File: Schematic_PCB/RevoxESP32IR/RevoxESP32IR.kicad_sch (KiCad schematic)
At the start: 27 parts, among them J1 SerialLink, J2 Conn_01x04, J3 Conn_01x10, J4 Conn_01x05, J5 Conn_01x04, J6 Conn_01x03, Q1 BC550, Q2 2N2222, Q3 BC550, U1 esp32-wemos-d1-mini, U2 TSOP331xx, U3 TTL-RS232 Modul, U6 FXMA108_THT

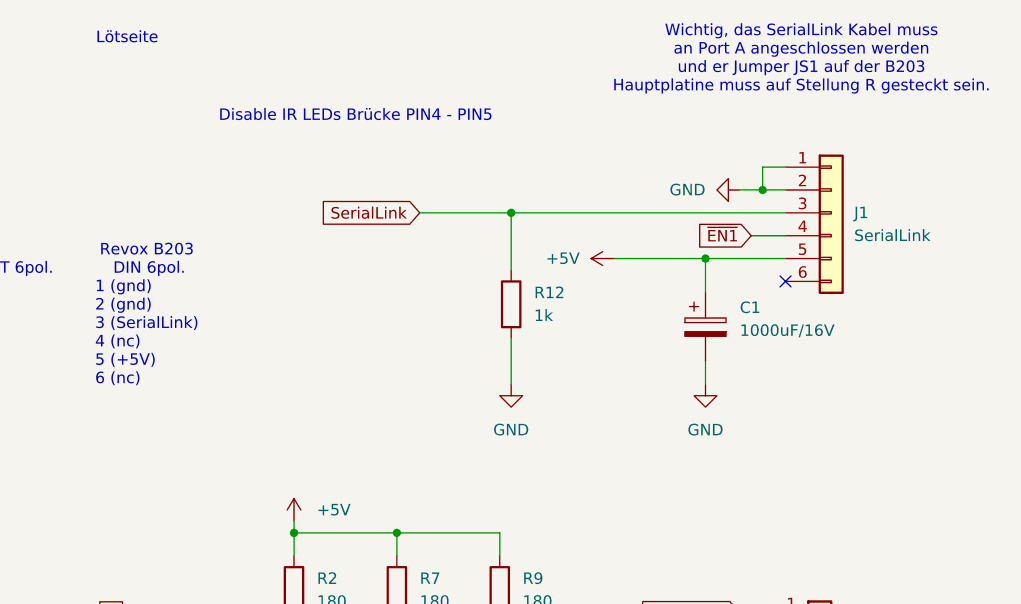
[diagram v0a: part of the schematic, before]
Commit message: Anpassung Schematic  und PCB.
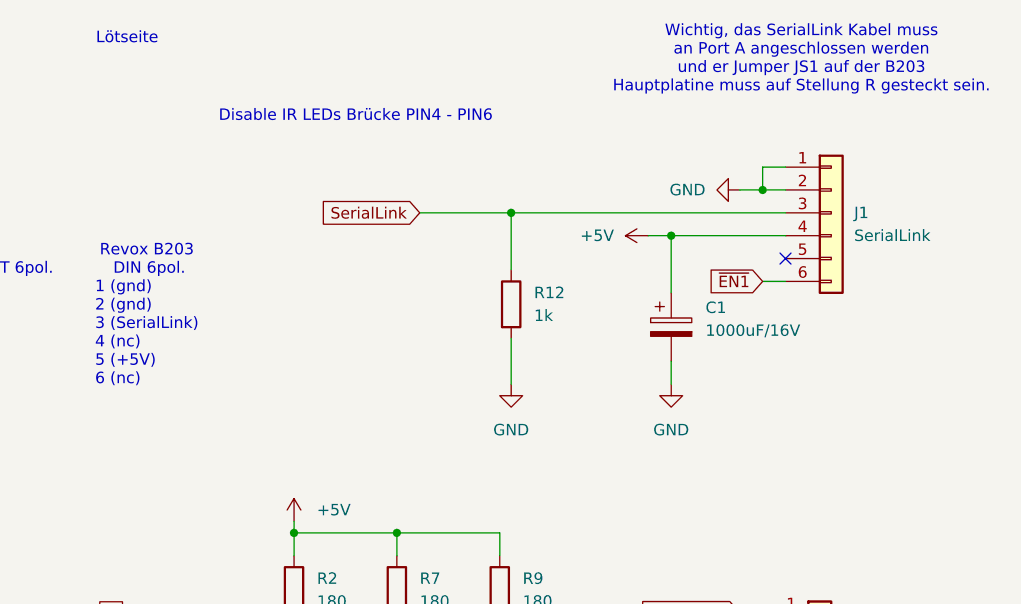
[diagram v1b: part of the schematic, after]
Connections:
- net +5V: now also J1.4 (Pin_4); no longer J1.5 (Pin_5)
- net ~{EN1}: now also J1.6 (Pin_6); no longer J1.4 (Pin_4)
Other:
- note added: "Disable IR LEDs Brücke PIN4 - PIN6"
- note removed: "Disable IR LEDs Brücke PIN4 - PIN5"
- moved on the sheet: C1
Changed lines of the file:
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@@
 		)
 	)
-	(text "Disable IR LEDs Brücke PIN4 - PIN5"
+	(text "Disable IR LEDs Brücke PIN4 - PIN6"
 		(exclude_from_sim no)
 		(at 210.058 24.892 0)
@@
 	)
 	(junction
-		(at 248.92 40.64)
-		(diameter 0)
-		(color 0 0 0 0)
-	)
-	(junction
 		(at 55.88 143.51)
 		(diameter 0)
@@
 	)
 	(junction
+		(at 245.11 38.1)
+		(diameter 0)
+		(color 0 0 0 0)
+	)
+	(junction
 		(at 214.63 71.12)
 		(diameter 0)
@@
 	)
 	(no_connect
-		(at 257.81 43.18)
-	)
-	(no_connect
 		(at 128.27 64.77)
 	)
@@
 	)
 	(no_connect
+		(at 257.81 40.64)
+	)
+	(no_connect
 		(at 156.21 171.45)
 	)
@@
 	(wire
 		(pts
-			(xy 238.76 40.64) (xy 248.92 40.64)
+			(xy 242.57 38.1) (xy 245.11 38.1)
 		)
 		(stroke
@@
 	(wire
 		(pts
-			(xy 248.92 40.64) (xy 248.92 44.45)
-		)
-		(stroke
-			(width 0)
-			(type default)
-		)
-	)
-	(wire
-		(pts
 			(xy 48.26 124.46) (xy 55.88 124.46)
 		)
@@
 	(wire
 		(pts
+			(xy 245.11 38.1) (xy 245.11 44.45)
+		)
+		(stroke
+			(width 0)
+			(type default)
+		)
+	)
+	(wire
+		(pts
 			(xy 193.04 100.33) (xy 195.58 100.33)
 		)
@@
 	(wire
 		(pts
-			(xy 248.92 52.07) (xy 248.92 54.61)
+			(xy 245.11 52.07) (xy 245.11 54.61)
 		)
 		(stroke
@@
 	(wire
 		(pts
-			(xy 254 38.1) (xy 257.81 38.1)
-		)
-		(stroke
-			(width 0)
-			(type default)
-		)
-	)
-	(wire
-		(pts
 			(xy 252.73 90.17) (xy 256.54 90.17)
 		)
@@
 	(wire
 		(pts
+			(xy 255.27 43.18) (xy 257.81 43.18)
+		)
+		(stroke
+			(width 0)
+			(type default)
+		)
+	)
+	(wire
+		(pts
 			(xy 168.91 116.84) (xy 168.91 119.38)
 		)
@@
 	(wire
 		(pts
+			(xy 245.11 38.1) (xy 257.81 38.1)
+		)
+		(stroke
+			(width 0)
+			(type default)
+		)
+	)
+	(wire
+		(pts
 			(xy 175.26 107.95) (xy 168.91 107.95)
 		)
@@
 		)
 	)
-	(wire
-		(pts
-			(xy 248.92 40.64) (xy 257.81 40.64)
-		)
-		(stroke
-			(width 0)
-			(type default)
-		)
-	)
 	(image
 		(at 248.158 151.892)
@@
 	(global_label "~{EN1}"
 		(shape input)
-		(at 254 38.1 180)
+		(at 255.27 43.18 180)
 		(fields_autoplaced yes)
 		(effects
@@
 		)
 		(property "Intersheetrefs" "${INTERSHEET_REFS}"
-			(at 247.3258 38.1 0)
+			(at 248.5958 43.18 0)
 			(hide yes)
 			(show_name no)
@@
 	(symbol
 		(lib_id "power:+5V")
-		(at 238.76 40.64 90)
+		(at 242.57 38.1 90)
 		(unit 1)
 		(body_style 1)
@@
 		(fields_autoplaced yes)
 		(property "Reference" "#PWR06"
-			(at 242.57 40.64 0)
+			(at 246.38 38.1 0)
 			(hide yes)
 			(show_name no)
@@
 		)
 		(property "Value" "+5V"
-			(at 234.95 40.6399 90)
+			(at 238.76 38.0999 90)
 			(show_name no)
 			(do_not_autoplace no)
@@
 		)
 		(property "Footprint" ""
-			(at 238.76 40.64 0)
+			(at 242.57 38.1 0)
 			(hide yes)
 			(show_name no)
@@
 		)
 		(property "Datasheet" ""
-			(at 238.76 40.64 0)
+			(at 242.57 38.1 0)
 			(hide yes)
 			(show_name no)
@@
 		)
 		(property "Description" "Power symbol creates a global label with name \"+5V\""
-			(at 238.76 40.64 0)
+			(at 242.57 38.1 0)
 			(hide yes)
 			(show_name no)
@@
 	(symbol
 		(lib_id "power:GND")
-		(at 248.92 54.61 0)
+		(at 245.11 54.61 0)
 		(unit 1)
 		(body_style 1)
@@
 		(fields_autoplaced yes)
 		(property "Reference" "#PWR08"
-			(at 248.92 60.96 0)
+			(at 245.11 60.96 0)
 			(hide yes)
 			(show_name no)
@@
 		)
 		(property "Value" "GND"
-			(at 248.92 59.69 0)
+			(at 245.11 59.69 0)
 			(show_name no)
 			(do_not_autoplace no)
@@
 		)
 		(property "Footprint" ""
-			(at 248.92 54.61 0)
+			(at 245.11 54.61 0)
 			(hide yes)
 			(show_name no)
@@
 		)
 		(property "Datasheet" ""
-			(at 248.92 54.61 0)
+			(at 245.11 54.61 0)
 			(hide yes)
 			(show_name no)
@@
 		)
 		(property "Description" "Power symbol creates a global label with name \"GND\" , ground"
-			(at 248.92 54.61 0)
+			(at 245.11 54.61 0)
 			(hide yes)
 			(show_name no)
@@
 	(symbol
 		(lib_id "Device:C_Polarized")
-		(at 248.92 48.26 0)
+		(at 245.11 48.26 0)
 		(unit 1)
 		(body_style 1)
@@
 		(fields_autoplaced yes)
 		(property "Reference" "C1"
-			(at 252.73 46.1009 0)
+			(at 248.92 46.1009 0)
 			(show_name no)
 			(do_not_autoplace no)
@@
 		)
 		(property "Value" "1000uF/16V"
-			(at 252.73 48.6409 0)
+			(at 248.92 48.6409 0)
 			(show_name no)
 			(do_not_autoplace no)
@@
 		)
 		(property "Footprint" "Capacitor_THT:CP_Radial_D8.0mm_P5.00mm"
-			(at 249.8852 52.07 0)
+			(at 246.0752 52.07 0)
 			(hide yes)
 			(show_name no)
@@
 		)
 		(property "Datasheet" ""
-			(at 248.92 48.26 0)
+			(at 245.11 48.26 0)
 			(hide yes)
 			(show_name no)
@@
 		)
 		(property "Description" "Polarized capacitor"
-			(at 248.92 48.26 0)
+			(at 245.11 48.26 0)
 			(hide yes)
 			(show_name no)

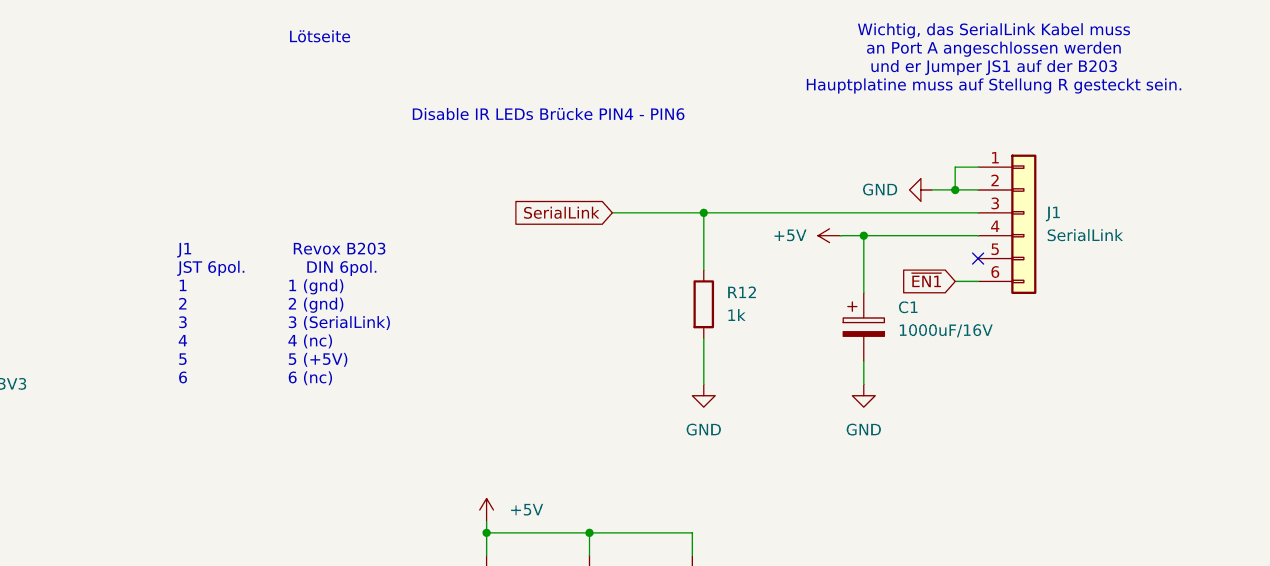
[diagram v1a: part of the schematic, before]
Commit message: Anpassung des Textes im Schaltplan.
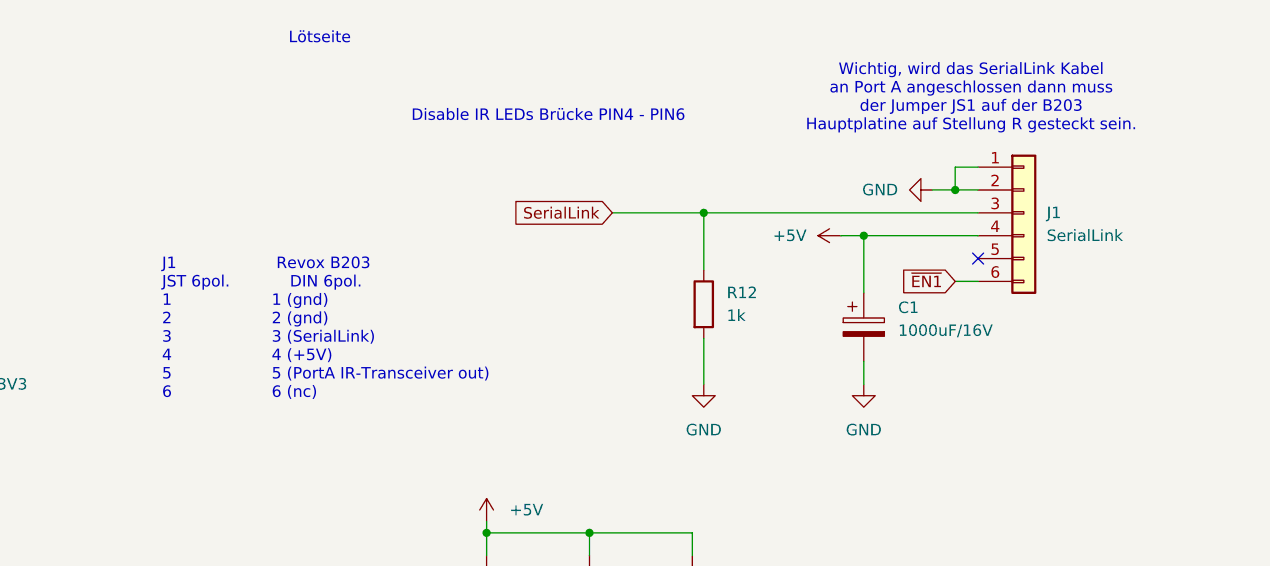
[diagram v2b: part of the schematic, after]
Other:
- note added: "J1 Revox B203 JST 6pol. DIN 6pol. 1 1 (gnd) 2 2 (gnd) 3 3 (SerialLink) 4 4 (+5V) 5 5 (PortA IR-Transceiver out) 6 6 (nc)"
- note added: "Wichtig, wird das SerialLink Kabel an Port A angeschlossen dann muss der Jumper JS1 auf der B203 Hauptplatine auf Stellung R gesteckt sein."
- note removed: "J1 Revox B203 JST 6pol. DIN 6pol. 1 1 (gnd) 2 2 (gnd) 3 3 (SerialLink) 4 4 (nc) 5 5 (+5V) 6 6 (nc)"
- note removed: "Wichtig, das SerialLink Kabel muss an Port A angeschlossen werden und er Jumper JS1 auf der B203 Hauptplatine muss auf Stellung R gesteckt sein."
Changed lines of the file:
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@@
 		)
 	)
-	(text "Wichtig, das SerialLink Kabel muss \nan Port A angeschlossen werden\nund er Jumper JS1 auf der B203\nHauptplatine muss auf Stellung R gesteckt sein."
+	(text "Wichtig, wird das SerialLink Kabel\nan Port A angeschlossen dann muss\nder Jumper JS1 auf der B203\nHauptplatine auf Stellung R gesteckt sein."
 		(exclude_from_sim no)
-		(at 259.588 18.542 0)
+		(at 257.048 22.86 0)
 		(effects
 			(font
@@
 		)
 	)
-	(text "J1					Revox B203\nJST 6pol.			DIN 6pol.\n1					1 (gnd)\n2					2 (gnd)\n3					3 (SerialLink)\n4					4 (nc)\n5					5 (+5V)\n6					6 (nc)"
+	(text "J1					Revox B203\nJST 6pol.			DIN 6pol.\n1					1 (gnd)\n2					2 (gnd)\n3					3 (SerialLink)\n4					4 (+5V)\n5					5 (PortA IR-Transceiver out)\n6					6 (nc)"
 		(exclude_from_sim no)
-		(at 168.91 46.99 0)
+		(at 167.132 48.514 0)
 		(effects
 			(font
